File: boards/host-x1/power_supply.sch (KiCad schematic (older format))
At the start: 0 parts

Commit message: Continued work on power supply
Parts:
- added C1, C10, C12, C2: 22 uF, symbol C
- added C11, C9: 100 uF, symbol C
- added C3, C5, C7: 10 uF, symbol C
- added C4: 0.1 uF, symbol C
- added C6, C8: 47 uF, symbol C
- added F1: 4A, symbol Fuse
- added J1: CONN_3_PWROUT, symbol CONN_3_PWROUT
- added L1, L3: SPM6530T-2R2M, symbol INDUCTOR_PWROUT
- added L2, L4: NRS6028T2R2NMGJ, symbol INDUCTOR_PWROUT
- added P1, P4, P5: TESTPOINT, symbol CONN_01X01
- added P2, P3: TESTCLIP, symbol CONN_01X01
- added R1: 1.33K, symbol R
- added R10: 464K, symbol R
- added R11: 649K, symbol R
- added R12: 324K, symbol R
- added R2, R4: 1K, symbol R
- added R3: 0, symbol R
- added R5: 255K, symbol R
- added R6: 232K, symbol R
- added R7: 806K, symbol R
- added R8, R9: 1.02M, symbol R
- added U1: OLK-T_3-W12P-C, symbol OLK-T_3-W12P-C
- added U2: XC7A100T-1FTG256C, symbol XC7AxT-xFTG256x
- added U3: LTC3374-QFN, symbol LTC3374-QFN
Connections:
- new net: R1.1, U1.6 (TRIM)
- new net 12V0_FUSED: C1.1, F1.1, U1.1 (EN), U1.2 (VIN)
- new net 12V0_UNFUSED: F1.2, J1.1 (P1)
- new net 1V0: C9.2, L1.1, R5.2, U2.E10 (VCCBRAM), U2.F11 (VCCBRAM), U2.F7 (VCCINT), U2.F9 (VCCINT), U2.G6 (VCCINT), U2.H9 (VCCINT), U2.J6 (VCCINT), U2.K9 (VCCINT), U2.L8 (VCCINT)
- new net 1V0_FB: R5.1, R9.2, U3.1 (FB1)
- new net 1V0_SW: L1.2, U3.3 (SW1), U3.4 (SW2), U3.9 (SW3)
- new net 1V2: C10.2, L2.1, R6.2
- new net 1V2_FB: R10.2, R6.1, U3.12 (FB4)
- new net 1V2_SW: L2.2, U3.10 (SW4)
- new net 1V8: C11.1, L3.1, R7.2, U2.A6 (VCCO_35), U2.B3 (VCCO_35), U2.D7 (VCCO_35), U2.E4 (VCCO_35), U2.F1 (VCCO_35), U2.F8 (VCCBATT), U2.G10 (VCCAUX), U2.G8 (VCCADC), U2.J10 (VCCAUX), U2.J2 (VCCO_35), U2.K11 (VCCAUX), U2.L10 (VCCAUX), U2.L16 (VCCO_14), U2.L6 (VCCO_0), U2.M13 (VCCO_14), U2.M3 (VCCO_34), U2.N10 (VCCO_14), U2.P7 (VCCO_14), U2.R14 (VCCO_14), U2.R4 (VCCO_34), U2.T1 (VCCO_34), U2.T11 (VCCO_14)
- new net 1V8_FB: R11.2, R7.1, U3.20 (FB5)
- new net 1V8_SW: L3.2, U3.22 (SW5), U3.23 (SW6), U3.28 (SW7)
- new net 3V3: C12.2, L4.1, R4.2, R8.2, U2.A16 (VCCO_15), U2.B13 (VCCO_15), U2.C10 (VCCO_15), U2.E14 (VCCO_15), U2.H15 (VCCO_15), U2.J12 (VCCO_15)
- new net 3V3_FB: R12.2, R8.1, U3.31 (FB8)
- new net 3V3_SW: L4.2, U3.29 (SW8)
- new net 5V0: C2.1, C3.1, C4.1, C5.1, C6.1, C7.1, C8.1, R2.1, R3.1, U1.4 (VOUT), U3.11 (VIN4), U3.13 (EN4), U3.17 (RT), U3.19 (EN5), U3.2 (VIN1), U3.21 (VIN5), U3.24 (VIN6), U3.25 (FB6), U3.26 (FB7), U3.27 (VIN7), U3.30 (VIN8), U3.32 (EN8), U3.34 (MODE), U3.35 (VCC), U3.38 (EN1), U3.5 (VIN2), U3.6 (FB2), U3.7 (FB3), U3.8 (VIN3)
- new net 5V0_PGOOD: P1.1 (P1), R2.2, U1.10 (PGOOD)
- new net 5V0_SENSE: R3.2, U1.5 (SENSE)
- new net BUCK_VTEMP: P4.1 (P1), U3.36 (TEMP)
- new net GND: C1.2, C10.1, C11.2, C12.1, C2.2, C3.2, C4.2, C5.2, C6.2, C7.2, C8.2, C9.1, J1.2 (PM), J1.3 (P3), P2.1 (P1), P3.1 (P1), R1.2, R10.1, R11.1, R12.1, R9.1, U1.3 (GND), U1.7 (GND), U2.A1 (GND), U2.A11 (GND), U2.B8 (GND), U2.C15 (GND), U2.C5 (GND), U2.D12 (GND), U2.D2 (GND), U2.E9 (GND), U2.F10 (GND), U2.F16 (GND), U2.F6 (GND), U2.G13 (GND), U2.G3 (GND), U2.G7 (GNDADC), U2.G9 (GND), U2.H6 (GND), U2.J11 (GND), U2.J9 (GND), U2.K14 (GND), U2.K4 (GND), U2.K6 (GND), U2.L1 (GND), U2.L11 (GND), U2.M8 (GND), U2.N15 (GND), U2.N5 (GND), U2.P12 (GND), U2.P2 (GND), U2.R9 (GND), U2.T16 (GND), U2.T6 (GND), U3.14 (EN3), U3.16 (SYNC), U3.18 (EN6), U3.33 (EN7), U3.37 (EN2), U3.PAD (GND)
- new net LTC_PGOOD: P5.1 (P1), R4.1, U3.15 (PGOOD_ALL)
- no-connect marks 0 -> 1
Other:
- note added: "Max 200 uF low-ESR caps on 5V0"

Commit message: Initial work on RAM
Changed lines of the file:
@@
 Sheet 2 5
 Title "STARSHIPRAIDER Single-Lane Host"
-Date "2017-05-04"
+Date "2017-05-06"
 Rev "0.1"
 Comp "Andrew D. Zonenberg"
@@
 	1    0    0    -1
 $EndComp
-Text Label 5100 1100 0    60   ~ 0
-5V0
 Wire Wire Line
 	4850 1100 5950 1100
@@
 Wire Wire Line
 	4850 900  5200 900
-Text Label 4850 600  2    60   ~ 0
-5V0
 Wire Wire Line
 	4850 600  5000 600
@@
 	0    1    1    0
 $EndComp
-Text Label 4300 3750 0    60   ~ 0
-1V0
 Wire Wire Line
 	4250 3750 4550 3750
@@
 Wire Wire Line
 	4950 3750 4850 3750
-Text Label 5350 3750 0    60   ~ 0
-GND
 Wire Wire Line
 	5350 3750 5250 3750
@@
 	0    1    1    0
 $EndComp
-Text Label 4300 5550 0    60   ~ 0
-1V2
 Wire Wire Line
 	4250 5550 4550 5550
@@
 	0    1    1    0
 $EndComp
-Text Label 4300 6150 0    60   ~ 0
-1V8
 Wire Wire Line
 	4250 6150 4550 6150
@@
 	0    1    1    0
 $EndComp
-Text Label 4300 7950 0    60   ~ 0
-3V3
 Wire Wire Line
 	4250 7950 4550 7950
@@
 	650  8600 650  8700
 Connection ~ 1100 8700
+Text HLabel 5350 3750 2    60   Output ~ 0
+GND
+Text HLabel 4250 3450 0    60   Output ~ 0
+1V0
+Wire Wire Line
+	4250 3450 4300 3450
+Wire Wire Line
+	4300 3450 4300 3750
+Connection ~ 4300 3750
+Text HLabel 4300 5300 0    60   Output ~ 0
+1V2
+Wire Wire Line
+	4300 5300 4350 5300
+Wire Wire Line
+	4350 5300 4350 5550
+Connection ~ 4350 5550
+Text HLabel 4400 5850 0    60   Output ~ 0
+1V8
+Wire Wire Line
+	4400 5850 4400 6150
+Connection ~ 4400 6150
+Text HLabel 4250 7700 0    60   Output ~ 0
+3V3
+Wire Wire Line
+	4250 7700 4300 7700
+Wire Wire Line
+	4300 7700 4300 7950
+Connection ~ 4300 7950
+Text Label 4850 600  2    60   ~ 0
+5V0
+Text HLabel 5200 1200 2    60   Output ~ 0
+5V0
+Wire Wire Line
+	5200 1200 5150 1200
+Wire Wire Line
+	5150 1200 5150 1100
+Connection ~ 5150 1100
 $EndSCHEMATC

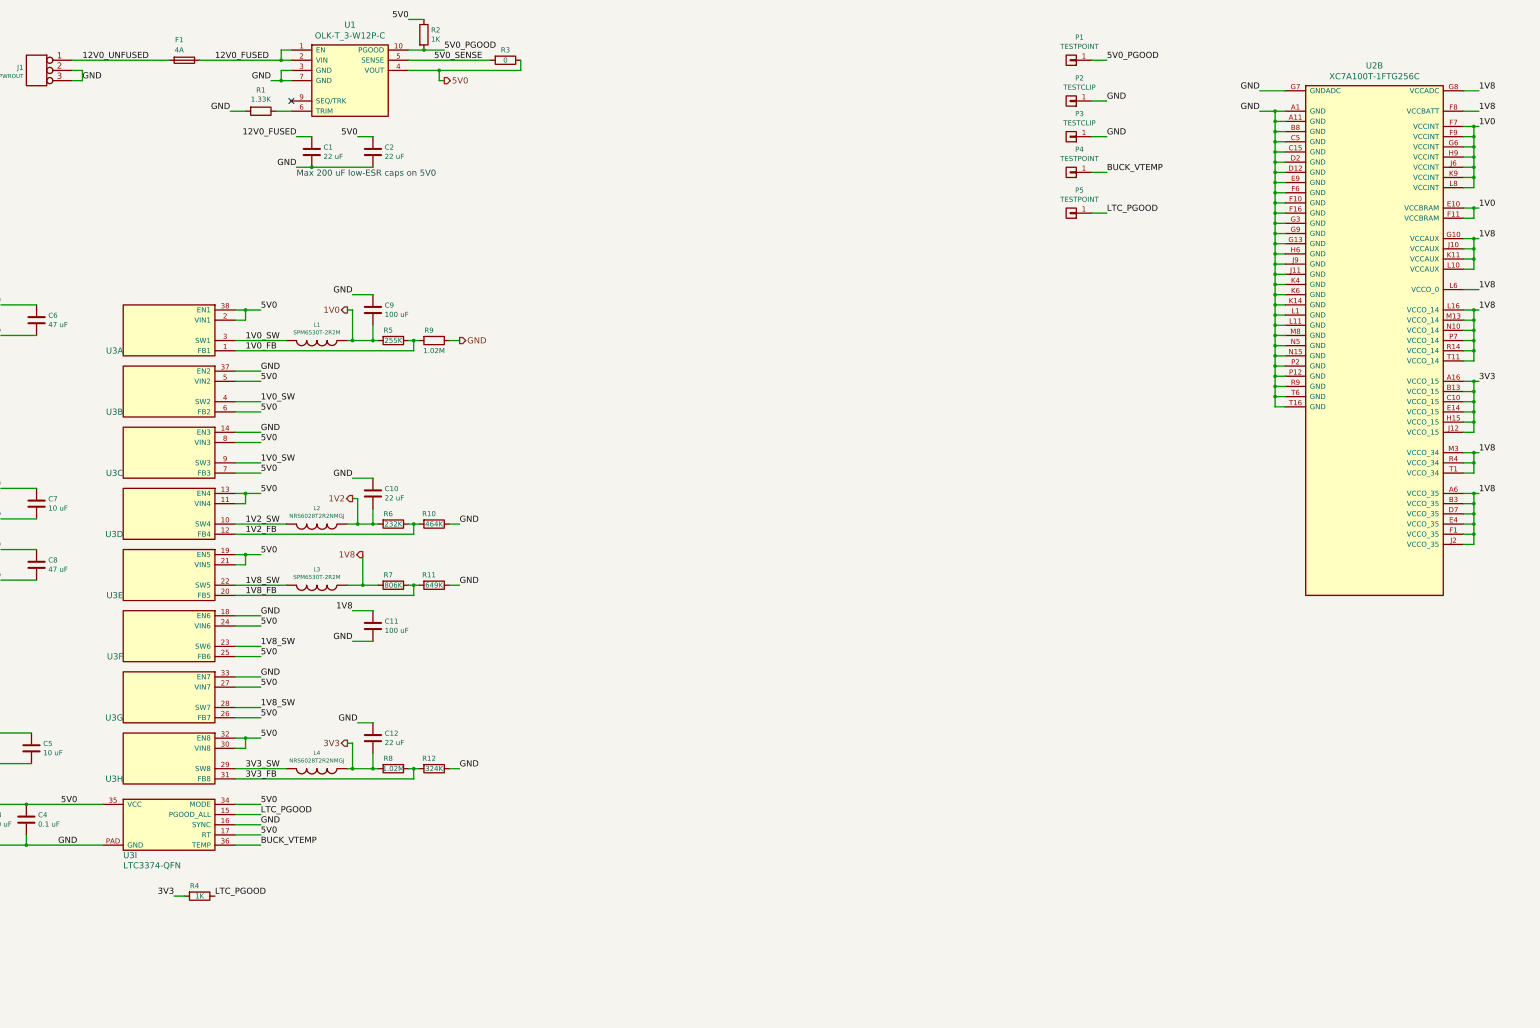
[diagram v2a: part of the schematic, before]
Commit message: Contineud work on x1 host schematic. Lots of decoupling, ethernet work, etc
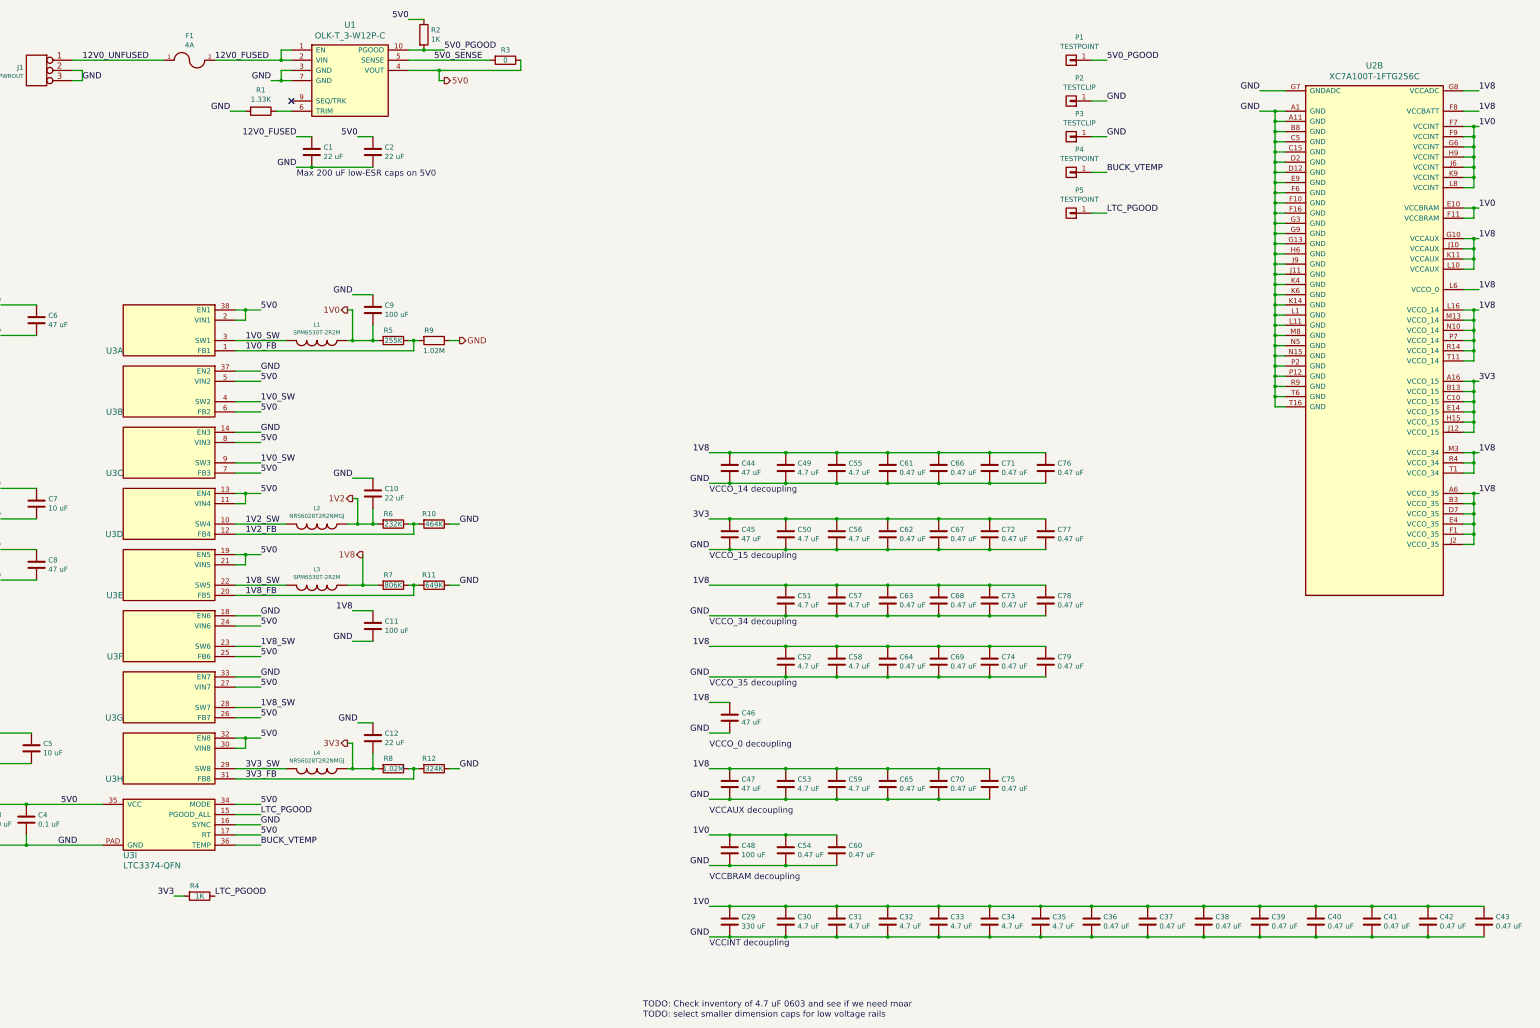
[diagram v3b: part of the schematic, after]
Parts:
- removed F1: 4A, symbol Fuse
- added C29: 330 uF, symbol C
- added C30, C31, C32, C33, C34, C35, C49, C50, C51, C52, C53, C55, C56, C57, C58, C59: 4.7 uF, symbol C
- added C36, C37, C38, C39, C40, C41, C42, C43, C54, C60, C61, C62, C63, C64, C65, C66, C67, C68, C69, C70, C71, C72, C73, C74, C75, C76, C77, C78, C79: 0.47 uF, symbol C
- added C44, C45, C46, C47: 47 uF, symbol C
- added C48: 100 uF, symbol C
- added F1: 4A, symbol FUSE_PWROUT
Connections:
- net 12V0_FUSED: now also F1.2
- net 12V0_UNFUSED: now also F1.1
- net 1V0: now also C29.1, C30.1, C31.1, C32.1, C33.1, C34.1, C35.1, C36.1, C37.1, C38.1, C39.1, C40.1, C41.1, C42.1, C43.1, C48.1, C54.1, C60.1
- net 1V8: now also C44.1, C46.1, C47.1, C49.1, C51.1, C52.1, C53.1, C55.1, C57.1, C58.1, C59.1, C61.1, C63.1, C64.1, C65.1, C66.1, C68.1, C69.1, C70.1, C71.1, C73.1, C74.1, C75.1, C76.1, C78.1, C79.1
- net 3V3: now also C45.1, C50.1, C56.1, C62.1, C67.1, C72.1, C77.1
- net GND: now also C29.2, C30.2, C31.2, C32.2, C33.2, C34.2, C35.2, C36.2, C37.2, C38.2, C39.2, C40.2, C41.2, C42.2, C43.2, C44.2, C45.2, C46.2, C47.2, C48.2, C49.2, C50.2, C51.2, C52.2, C53.2, C54.2, C55.2, C56.2, C57.2, C58.2, C59.2, C60.2, C61.2, C62.2, C63.2, C64.2, C65.2, C66.2, C67.2, C68.2, C69.2, C70.2, C71.2, C72.2, C73.2, C74.2, C75.2, C76.2, C77.2, C78.2, C79.2
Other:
- note added: "TODO: Check inventory of 4.7 uF 0603 and see if we need moar"
- note added: "TODO: select smaller dimension caps for low voltage rails"
- note added: "VCCAUX decoupling"
- note added: "VCCBRAM decoupling"
- note added: "VCCINT decoupling"
- note added: "VCCO_0 decoupling"
- note added: "VCCO_14 decoupling"
- note added: "VCCO_15 decoupling"
- note added: "VCCO_34 decoupling"
- note added: "VCCO_35 decoupling"
